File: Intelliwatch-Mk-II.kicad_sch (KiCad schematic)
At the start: 74 parts, among them J1 Voltmeter Probes, J2 DC Power Input, J3 USB_C_Receptacle_USB2.0_16P, J4 Flashlight Terminals, J5 CONN LCD 1.8 TFT SPI, J6 Conn 7S-4D HW-069 I2C, Q1 NDS331N, SW1 PWR SPST, SW2 EN Button, SW3 LCD LED SPST, SW4 Cherry MX Keyswitch, SW5 Cherry MX Keyswitch, SW6 Cherry MX Keyswitch, SW7 Cherry MX Keyswitch, SW8 PROG Button, U1 SN74HC02N, U2 MCP3421A0T-ECH, U3 74AHC1G04GW_125, U4 74AHC1G04GW_125, U5 LM7805, U6 CH340C, U7 SY8120IABC, U8 QMC5883L, U9 ESP32-WROOM-32UE

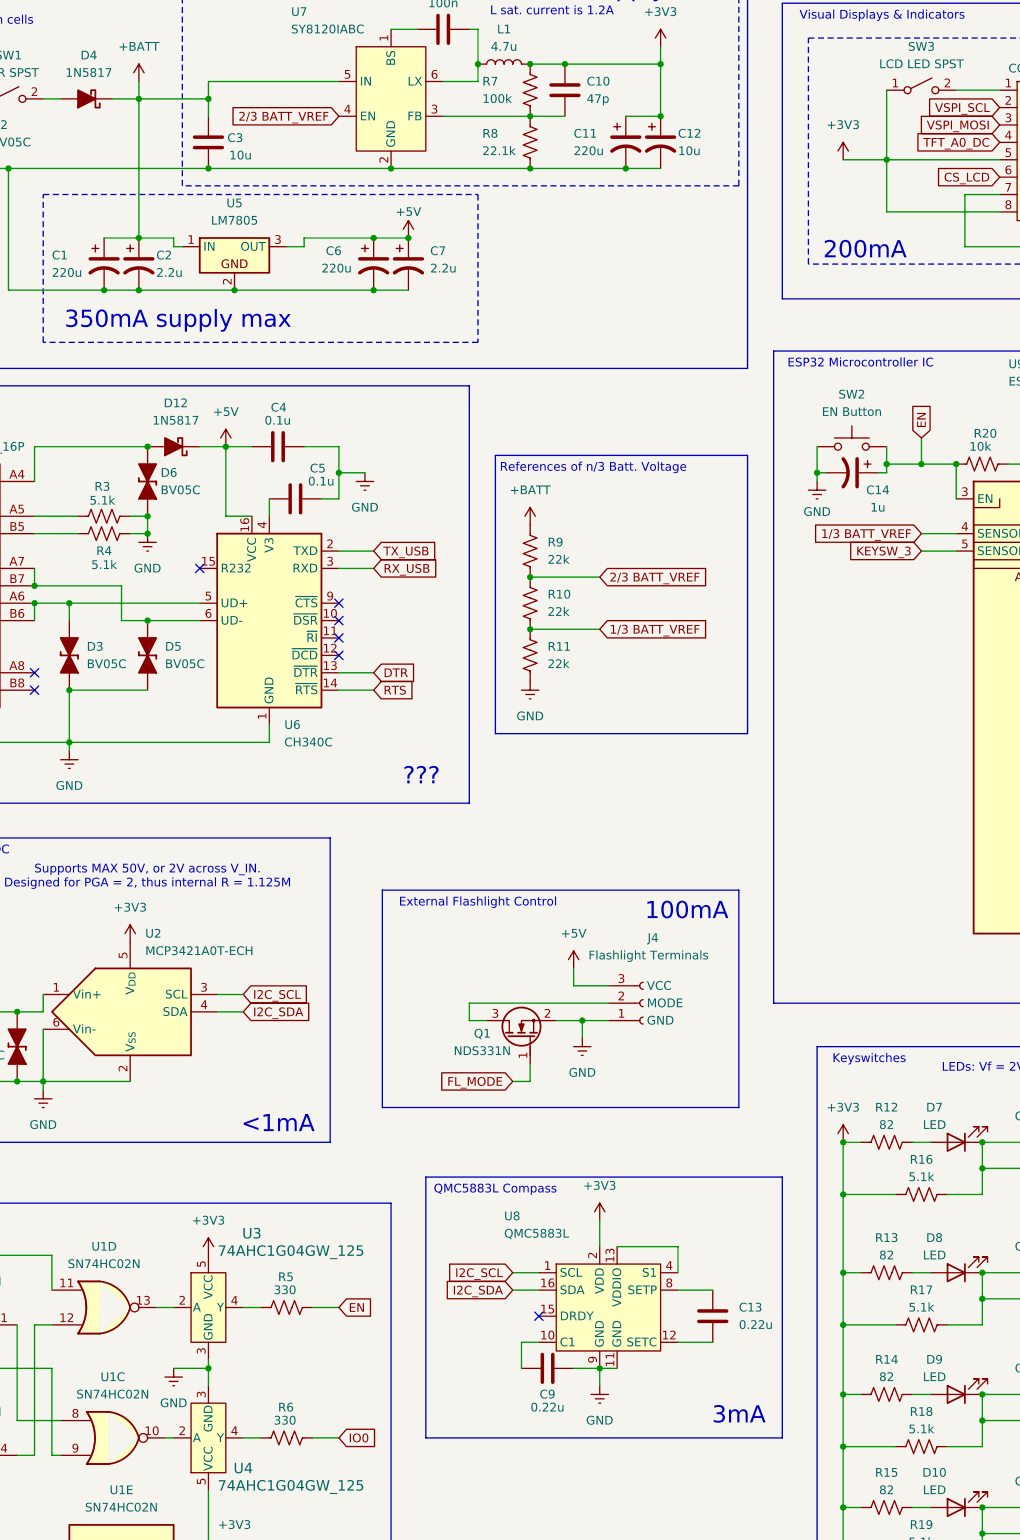
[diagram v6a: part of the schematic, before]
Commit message: ADDED LCSC part #s for all applicable components except for resistors. TODO WIP add resistor LCSC part #s.
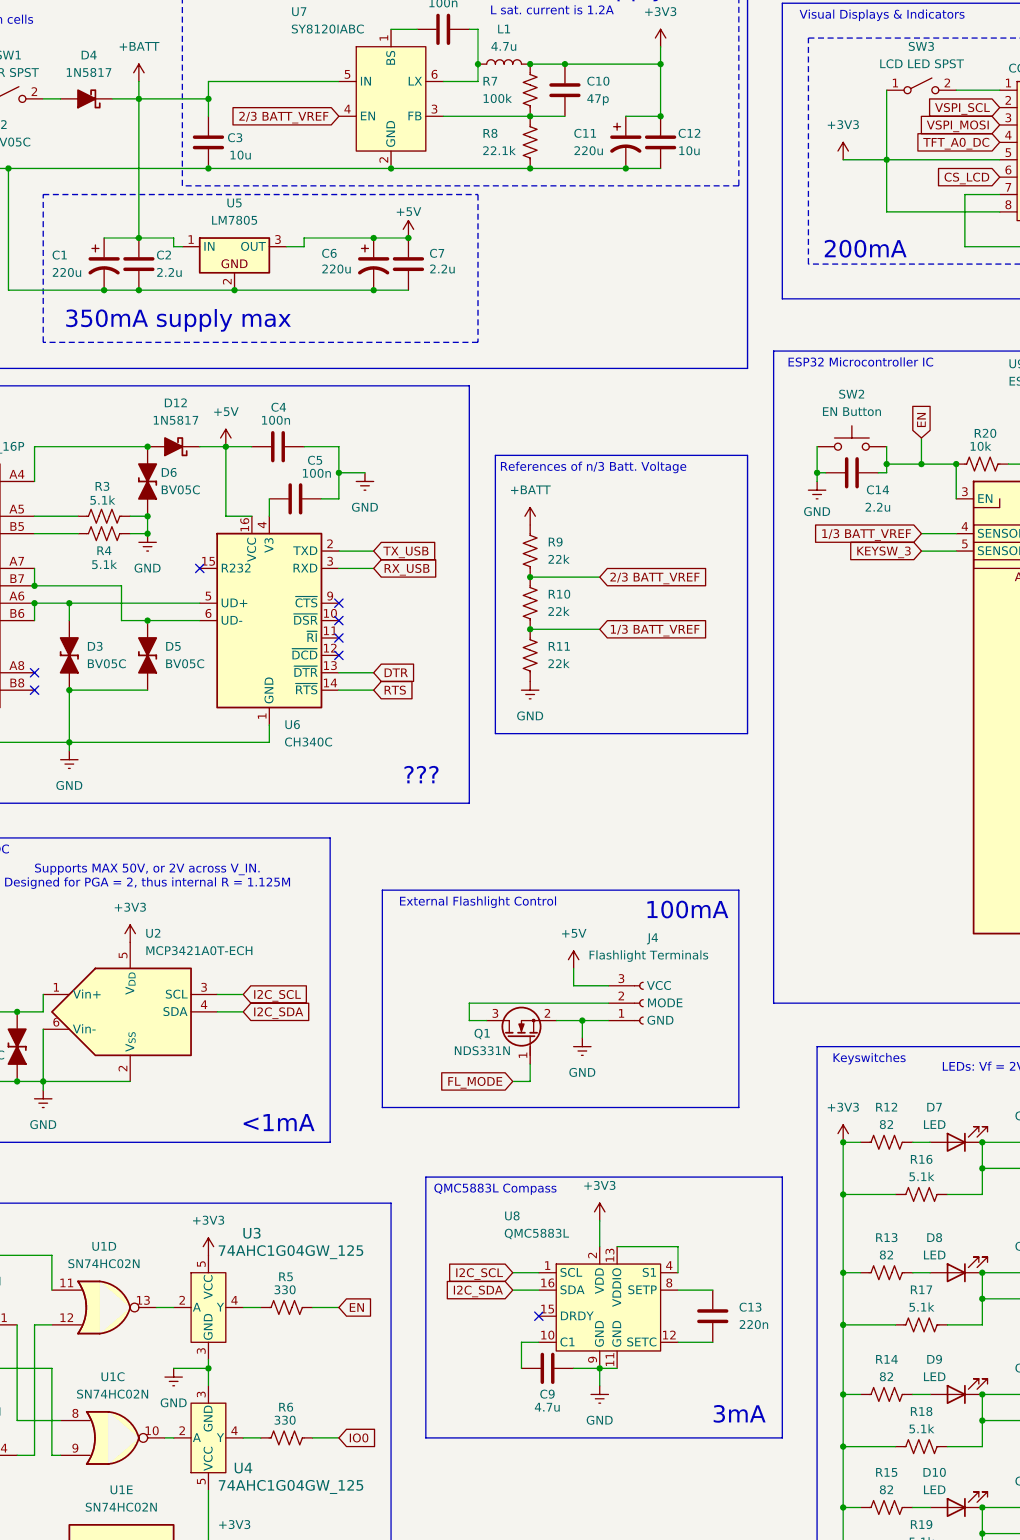
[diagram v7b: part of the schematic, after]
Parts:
- C1, C11, C6: LCSC Part # (none) -> n/a
- C10: footprint (none) -> Capacitor_SMD:C_0603_1608Metric; LCSC Part # (none) -> C882552
- C12: footprint (none) -> Capacitor_SMD:C_0805_2012Metric; symbol Device:C_Polarized_US -> Device:C; LCSC Part # (none) -> C440198
- C13: value 0.22u -> 220n; footprint (none) -> Capacitor_SMD:C_1206_3216Metric; LCSC Part # (none) -> C161277
- C14: value 1u -> 2.2u; footprint (none) -> Capacitor_SMD:C_0603_1608Metric; symbol Device:C_Polarized_US -> Device:C; LCSC Part # (none) -> C415535
- C2, C7: footprint (none) -> Capacitor_SMD:C_0603_1608Metric; symbol Device:C_Polarized_US -> Device:C; LCSC Part # (none) -> C415535
- C3: footprint (none) -> Capacitor_SMD:C_0805_2012Metric; LCSC Part # (none) -> C440198
- C4, C5: value 0.1u -> 100n; footprint (none) -> Capacitor_SMD:C_1206_3216Metric; LCSC Part # (none) -> C97946
- C8: footprint (none) -> Capacitor_SMD:C_1206_3216Metric; LCSC Part # (none) -> C97946
- C9: value 0.22u -> 4.7u; footprint (none) -> Capacitor_SMD:C_0805_2012Metric; LCSC Part # (none) -> C437557
- L1: footprint (none) -> Inductor_SMD:L_7.3x7.3_H3.5; LCSC Part # (none) -> C136201
- R1: LCSC Part # (none) -> C5200509
- SW1, SW3: footprint (none) -> ZCustomFootprints:Standard IO Holes
- U1: LCSC Part # (none) -> C2897
- U2: LCSC Part # (none) -> C29454
- U3, U4: LCSC Part # (none) -> C12484
- U5: footprint PCM_Package_TO_SOT_THT_AKL:TO-220-3_Vertical -> PCM_Package_TO_SOT_THT_AKL:TO-220-3_Horizontal_TabDown; LCSC Part # (none) -> n/a
- U6: LCSC Part # (none) -> C84681
- U7: LCSC Part # (none) -> C479076
- U8: LCSC Part # (none) -> C976032
- U9: LCSC Part # (none) -> C701346
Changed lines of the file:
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@@
 			)
 		)
-		(property "LCSC Part #" ""
+		(property "LCSC Part #" "C2897"
 			(at 38.1 214.63 0)
 			(effects
@@
 			)
 		)
-		(property "LCSC Part #" ""
+		(property "LCSC Part #" "n/a"
 			(at 58.42 59.69 0)
 			(effects
@@
 			)
 		)
-		(property "LCSC Part #" ""
+		(property "LCSC Part #" "C5200509"
 			(at 35.56 165.1 0)
 			(effects
@@
 			)
 		)
-		(property "LCSC Part #" ""
+		(property "LCSC Part #" "n/a"
 			(at 134.62 41.91 0)
 			(effects
@@
 			)
 		)
-		(property "LCSC Part #" ""
+		(property "LCSC Part #" "C479076"
 			(at 100.33 35.56 0)
 			(effects
@@
 			)
 		)
-		(property "Footprint" ""
+		(property "Footprint" "Capacitor_SMD:C_0603_1608Metric"
 			(at 126.6952 38.1 0)
 			(effects
@@
 			)
 		)
-		(property "LCSC Part #" ""
+		(property "LCSC Part #" "C882552"
 			(at 125.73 34.29 0)
 			(effects
@@
 	)
 	(symbol
-		(lib_id "Device:C_Polarized_US")
+		(lib_id "Device:C")
 		(at 139.7 41.91 0)
 		(unit 1)
@@
 			)
 		)
-		(property "Footprint" ""
-			(at 139.7 41.91 0)
+		(property "Footprint" "Capacitor_SMD:C_0805_2012Metric"
+			(at 140.6652 45.72 0)
 			(effects
 				(font
@@
 			)
 		)
-		(property "Description" "Polarized capacitor, US symbol"
+		(property "Description" "Unpolarized capacitor"
 			(at 139.7 41.91 0)
 			(effects
@@
 			)
 		)
-		(property "LCSC Part #" ""
+		(property "LCSC Part #" "C440198"
 			(at 139.7 41.91 0)
 			(effects
@@
 			)
 		)
-		(property "Value" "0.22u"
+		(property "Value" "4.7u"
 			(at 123.19 226.695 90)
 			(effects
@@
 			)
 		)
-		(property "Footprint" ""
+		(property "Footprint" "Capacitor_SMD:C_0805_2012Metric"
 			(at 127 220.0148 0)
 			(effects
@@
 			)
 		)
-		(property "LCSC Part #" ""
+		(property "LCSC Part #" "C437557"
 			(at 123.19 220.98 0)
 			(effects
@@
 	)
 	(symbol
-		(lib_id "Device:C_Polarized_US")
+		(lib_id "Device:C")
 		(at 63.5 59.69 0)
 		(unit 1)
@@
 			)
 		)
-		(property "Footprint" ""
-			(at 63.5 59.69 0)
+		(property "Footprint" "Capacitor_SMD:C_0603_1608Metric"
+			(at 64.4652 63.5 0)
 			(effects
 				(font
@@
 			)
 		)
-		(property "Description" "Polarized capacitor, US symbol"
+		(property "Description" "Unpolarized capacitor"
 			(at 63.5 59.69 0)
 			(effects
@@
 			)
 		)
-		(property "LCSC Part #" ""
+		(property "LCSC Part #" "C415535"
 			(at 63.5 59.69 0)
 			(effects
@@
 			)
 		)
-		(property "LCSC Part #" ""
+		(property "LCSC Part #" "C12484"
 			(at 73.66 231.14 0)
 			(effects
@@
 			)
 		)
-		(property "Footprint" ""
+		(property "Footprint" "ZCustomFootprints:Standard IO Holes"
 			(at 177.8 34.29 0)
 			(effects
@@
 	)
 	(symbol
-		(lib_id "Device:C_Polarized_US")
+		(lib_id "Device:C")
 		(at 102.87 59.69 0)
 		(unit 1)
@@
 		(dnp no)
 		(property "Reference" "C7"
-			(at 106.045 57.785 0)
+			(at 105.918 58.166 0)
 			(effects
 				(font
@@
 		)
 		(property "Value" "2.2u"
-			(at 106.045 60.325 0)
+			(at 105.918 60.452 0)
 			(effects
 				(font
@@
 			)
 		)
-		(property "Footprint" ""
-			(at 102.87 59.69 0)
+		(property "Footprint" "Capacitor_SMD:C_0603_1608Metric"
+			(at 103.8352 63.5 0)
 			(effects
 				(font
@@
 			)
 		)
-		(property "Description" "Polarized capacitor, US symbol"
+		(property "Description" "Unpolarized capacitor"
 			(at 102.87 59.69 0)
 			(effects
@@
 			)
 		)
-		(property "LCSC Part #" ""
+		(property "LCSC Part #" "C415535"
 			(at 102.87 59.69 0)
 			(effects
@@
 			)
 		)
-		(property "Footprint" ""
+		(property "Footprint" "Inductor_SMD:L_7.3x7.3_H3.5"
 			(at 116.84 30.48 0)
 			(effects
@@
 			)
 		)
-		(property "LCSC Part #" ""
+		(property "LCSC Part #" "C136201"
 			(at 116.84 30.48 0)
 			(effects
@@
 			)
 		)
-		(property "LCSC Part #" ""
+		(property "LCSC Part #" "C2897"
 			(at 38.1 233.68 0)
 			(effects
@@
 			)
 		)
-		(property "LCSC Part #" ""
+		(property "LCSC Part #" "C2897"
 			(at 58.42 212.09 0)
 			(effects
@@
 			)
 		)
-		(property "LCSC Part #" ""
+		(property "LCSC Part #" "C976032"
 			(at 130.81 212.09 0)
 			(effects
@@
 			)
 		)
-		(property "Value" "0.22u"
+		(property "Value" "220n"
 			(at 151.13 214.6299 0)
 			(effects
@@
 			)
 		)
-		(property "Footprint" ""
+		(property "Footprint" "Capacitor_SMD:C_1206_3216Metric"
 			(at 148.2852 217.17 0)
 			(effects
@@
 			)
 		)
-		(property "LCSC Part #" ""
+		(property "LCSC Part #" "C161277"
 			(at 147.32 213.36 0)
 			(effects
@@
 			)
 		)
-		(property "LCSC Part #" ""
+		(property "LCSC Part #" "C701346"
 			(at 198.12 124.46 0)
 			(effects
@@
 			)
 		)
-		(property "Footprint" ""
+		(property "Footprint" "ZCustomFootprints:Standard IO Holes"
 			(at 44.45 35.56 0)
 			(effects
@@
 			)
 		)
-		(property "Footprint" "PCM_Package_TO_SOT_THT_AKL:TO-220-3_Vertical"
+		(property "Footprint" "PCM_Package_TO_SOT_THT_AKL:TO-220-3_Horizontal_TabDown"
 			(at 77.47 57.15 0)
 			(effects
@@
 			)
 		)
-		(property "LCSC Part #" ""
+		(property "LCSC Part #" "n/a"
 			(at 77.47 57.15 0)
 			(effects
@@
 			)
 		)
-		(property "LCSC Part #" ""
+		(property "LCSC Part #" "C12484"
 			(at 73.66 212.09 0)
 			(effects
@@
 			)
 		)
-		(property "Footprint" ""
+		(property "Footprint" "Capacitor_SMD:C_1206_3216Metric"
 			(at 111.76 24.4348 0)
 			(effects
@@
 			)
 		)
-		(property "LCSC Part #" ""
+		(property "LCSC Part #" "C97946"
 			(at 107.95 25.4 0)
 			(effects
@@
 	)
 	(symbol
-		(lib_id "Device:C_Polarized_US")
+		(lib_id "Device:C")
 		(at 167.64 90.17 270)
 		(unit 1)
@@
 			)
 		)
-		(property "Value" "1u"
+		(property "Value" "2.2u"
 			(at 171.45 95.25 90)
 			(effects
@@
 			)
 		)
-		(property "Footprint" ""
-			(at 167.64 90.17 0)
+		(property "Footprint" "Capacitor_SMD:C_0603_1608Metric"
+			(at 163.83 91.1352 0)
 			(effects
 				(font
@@
 			)
 		)
-		(property "Description" "Polarized capacitor, US symbol"
+		(property "Description" "Unpolarized capacitor"
 			(at 167.64 90.17 0)
 			(effects
@@
 			)
 		)
-		(property "LCSC Part #" ""
+		(property "LCSC Part #" "C415535"
 			(at 167.64 90.17 0)
 			(effects
@@
 		(dnp no)
 		(property "Reference" "C5"
-			(at 90.805 89.535 90)
+			(at 90.424 88.392 90)
 			(effects
 				(font
@@
 			)
 		)
-		(property "Value" "0.1u"
-			(at 92.075 91.44 90)
+		(property "Value" "100n"
+			(at 91.694 90.297 90)
 			(effects
 				(font
@@
 			)
 		)
-		(property "Footprint" ""
+		(property "Footprint" "Capacitor_SMD:C_1206_3216Metric"
 			(at 90.17 93.0148 0)
 			(effects
@@
 			)
 		)
-		(property "LCSC Part #" ""
+		(property "LCSC Part #" "C97946"
 			(at 86.36 93.98 0)
 			(effects
@@
 			)
 		)
-		(property "LCSC Part #" ""
+		(property "LCSC Part #" "C29454"
 			(at 62.23 168.91 0)
 			(effects
@@
 			)
 		)
-		(property "LCSC Part #" ""
+		(property "LCSC Part #" "C2897"
 			(at 59.69 231.14 0)
 			(effects
@@
 		(dnp no)
 		(property "Reference" "C6"
-			(at 90.805 57.785 0)
+			(at 90.17 58.166 0)
 			(effects
 				(font
@@
 		)
 		(property "Value" "220u"
-			(at 90.17 60.325 0)
+			(at 90.17 60.452 0)
 			(effects
 				(font
@@
 			)
 		)
-		(property "LCSC Part #" ""
+		(property "LCSC Part #" "n/a"
 			(at 97.79 59.69 0)
 			(effects
@@
 			)
 		)
-		(property "LCSC Part #" ""
+		(property "LCSC Part #" "C84681"
 			(at 82.55 111.76 0)
 			(effects
@@
 			)
 		)
-		(property "Footprint" ""
+		(property "Footprint" "Capacitor_SMD:C_0805_2012Metric"
 			(at 72.6948 45.72 0)
 			(effects
@@
 			)
 		)
-		(property "LCSC Part #" ""
+		(property "LCSC Part #" "C440198"
 			(at 73.66 41.91 0)
 			(effects
@@
 			)
 		)
-		(property "Value" "0.1u"
+		(property "Value" "100n"
 			(at 85.725 82.55 90)
 			(effects
@@
 			)
 		)
-		(property "Footprint" ""
+		(property "Footprint" "Capacitor_SMD:C_1206_3216Metric"
 			(at 87.63 85.3948 0)
 			(effects
@@
 			)
 		)
-		(property "LCSC Part #" ""
+		(property "LCSC Part #" "C97946"
 			(at 83.82 86.36 0)
 			(effects
@@
 			)
 		)
-		(property "LCSC Part #" ""
+		(property "LCSC Part #" "C2897"
 			(at 60.96 248.92 0)
 			(effects
